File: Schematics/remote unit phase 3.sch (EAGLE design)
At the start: 18 parts, among them IC4 317T, M1 ARDUINO-PRO-MINI-5.0V, M2 WIRELESS-NRF24L01, X2 22-23-2021

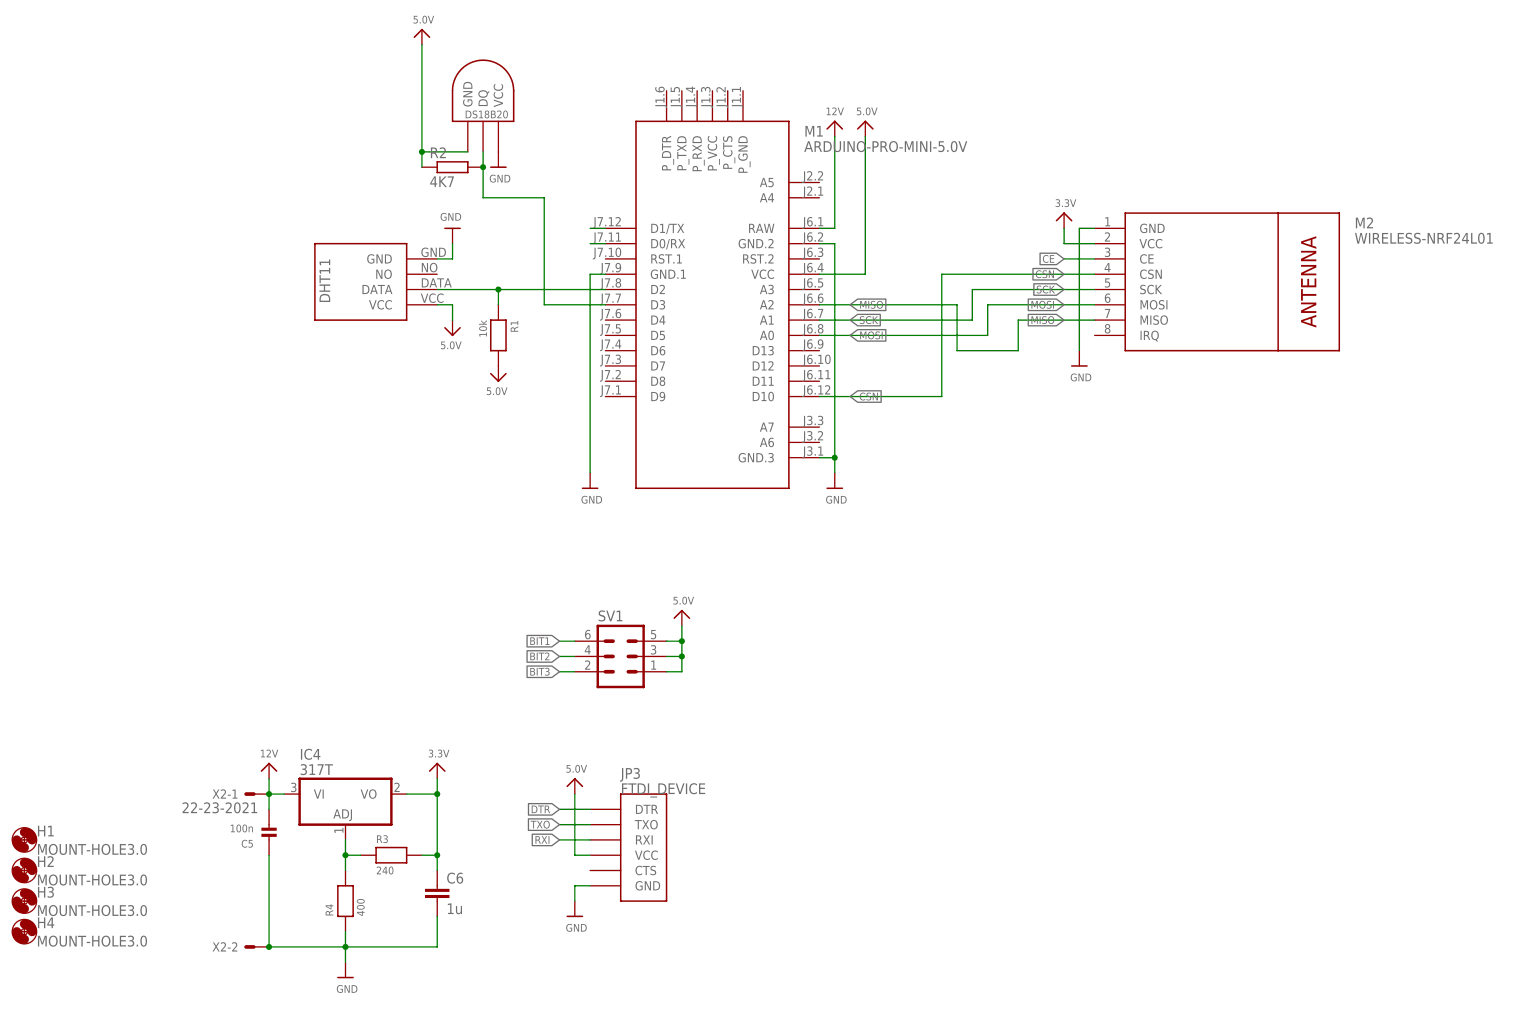
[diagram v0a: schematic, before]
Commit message: rettelse af sensorafsnit, og sidste schematics
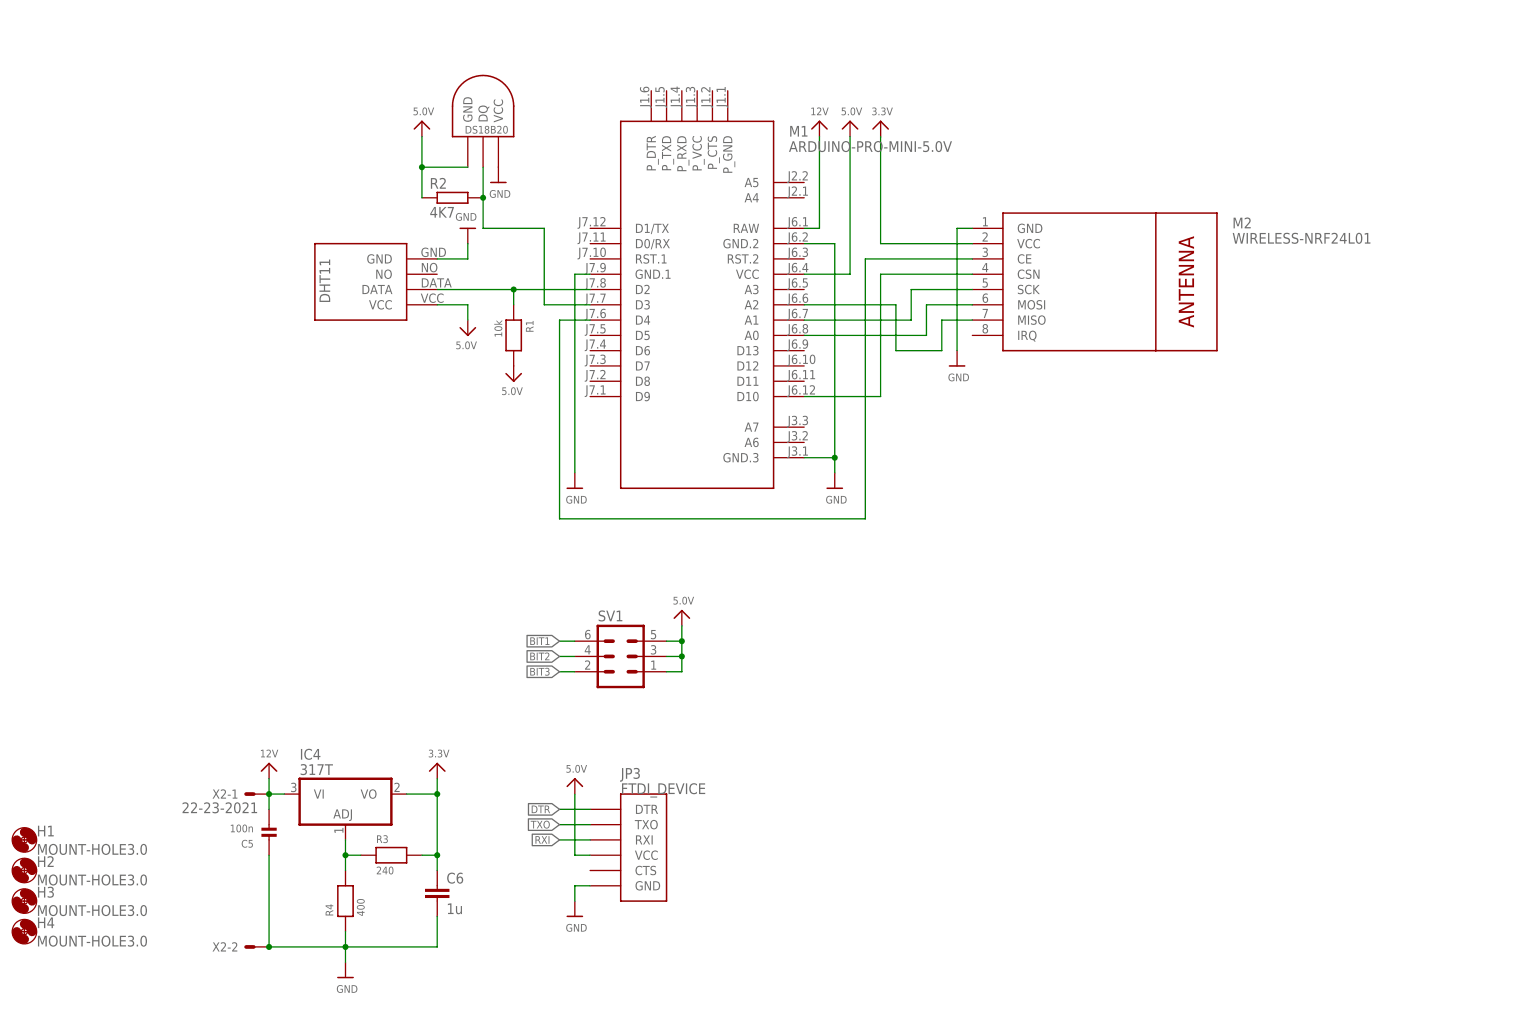
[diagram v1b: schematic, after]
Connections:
- net CE: now also M1.D4
- net GND: now also U$14.VCC
- net RXI: no longer M1.D0/RX
- net TXO: no longer M1.D1/TX
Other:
- moved on the sheet: M1, M2, R1, R2
